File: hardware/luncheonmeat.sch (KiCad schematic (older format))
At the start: 55 parts, among them J1 USB_B_Micro, J2 Conn_02x03_Odd_Even, Q1 Q_PMOS_DGS, Q2 Q_PMOS_DGS, Q3 Q_PMOS_DGS, SW1 SW_Push, SW10 7, SW11 4, SW12 1, SW13 *, SW2 9, SW3 6, SW4 3, SW5 #, SW6 8, SW7 5, SW8 2, SW9 0, U1 ATmega328PB-AU, U2 lsd100bag-101-20, U3 lsd100bag-101-20, U4 lsd100bag-101-20, U5 FT230XS, Y1 16MHz

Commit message: Fix schematic, new board layout
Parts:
- removed C1, C10, C8, C9: 100n, Capacitor_SMD:C_0603_1608Metric_Pad1.05x0.95mm_HandSolder, symbol Device:C
- removed C2, C3: 22p, Capacitor_SMD:C_0603_1608Metric_Pad1.05x0.95mm_HandSolder, symbol Device:C
- removed D1: LED, Diode_SMD:D_0603_1608Metric_Pad1.05x0.95mm_HandSolder, symbol Device:LED
- removed J2: Conn_02x03_Odd_Even, Connector_PinHeader_2.54mm:PinHeader_2x03_P2.54mm_Vertical, symbol Connector_Generic:Conn_02x03_Odd_Even
- removed JP? (x2): Jumper_2_Open, symbol Jumper:Jumper_2_Open
- removed R1: 100k, Resistor_SMD:R_0603_1608Metric_Pad1.05x0.95mm_HandSolder, symbol Device:R
- removed R10, R11, R12, R13, R14, R15, R16, R7, R8, R9: 300R, Resistor_SMD:R_0603_1608Metric_Pad1.05x0.95mm_HandSolder, symbol Device:R
- removed R2, R3, R4: 1k, Resistor_SMD:R_0603_1608Metric_Pad1.05x0.95mm_HandSolder, symbol Device:R
- removed Y1: 16MHz, Crystal:Crystal_HC49-4H_Vertical, symbol Device:Crystal_Small
- added C1: 10nF, Capacitor_SMD:C_0805_2012Metric_Pad1.18x1.45mm_HandSolder, symbol Device:C_Small
- added C10, C6, C7, C8, C9: 100nF, Capacitor_SMD:C_0805_2012Metric_Pad1.18x1.45mm_HandSolder, symbol Device:C_Small
- added C12, C13: 22pF, Capacitor_SMD:C_0603_1608Metric_Pad1.08x0.95mm_HandSolder, symbol Device:C_Small
- added D1: G, LED_SMD:LED_0805_2012Metric_Castellated, symbol Device:LED_Small
- added D2: R, LED_SMD:LED_0805_2012Metric_Castellated, symbol Device:LED_Small
- added D3: Y, LED_SMD:LED_0805_2012Metric_Castellated, symbol Device:LED_Small
- added D4: D_Small, Diode_SMD:D_0805_2012Metric, symbol Device:D_Small
- added H1, H2, H3, H4, H5, H6: MH, MountingHole:MountingHole_3.2mm_M3_DIN965, symbol Mechanical:MountingHole
- added J2: AVR-ISP-6, Connector_IDC:IDC-Header_2x03_P2.54mm_Vertical, symbol Connector:AVR-ISP-6
- added R1: 1M, Resistor_SMD:R_0805_2012Metric_Pad1.20x1.40mm_HandSolder, symbol Device:R_Small
- added R10, R11, R12, R13, R14, R15, R16, R2, R7, R9: 300R, Resistor_SMD:R_0805_2012Metric_Pad1.20x1.40mm_HandSolder, symbol Device:R_Small
- added R17, R18: 0R, Resistor_SMD:R_0805_2012Metric_Pad1.20x1.40mm_HandSolder, symbol Device:R_Small
- added R19, R20, R21: 1k, Resistor_SMD:R_0805_2012Metric_Pad1.20x1.40mm_HandSolder, symbol Device:R_Small
- added R3, R4: 1.5k, Resistor_SMD:R_0805_2012Metric_Pad1.20x1.40mm_HandSolder, symbol Device:R_Small
- added R8: 10k, Resistor_SMD:R_0805_2012Metric_Pad1.20x1.40mm_HandSolder, symbol Device:R_Small
- added Y1: 8MHz, Crystal:Crystal_SMD_0603-4Pin_6.0x3.5mm_HandSoldering, symbol Device:Crystal_GND2_Small
- C2: renamed from C4; value 10n -> 10nF; footprint Capacitor_SMD:C_0603_1608Metric_Pad1.05x0.95mm_HandSolder -> Capacitor_SMD:C_0805_2012Metric_Pad1.18x1.45mm_HandSolder
- C3: renamed from C5; footprint Capacitor_SMD:C_0603_1608Metric_Pad1.05x0.95mm_HandSolder -> Capacitor_SMD:C_0805_2012Metric_Pad1.18x1.45mm_HandSolder
- C4: renamed from C6; footprint Capacitor_SMD:C_0603_1608Metric_Pad1.05x0.95mm_HandSolder -> Capacitor_SMD:C_0805_2012Metric_Pad1.18x1.45mm_HandSolder
- C5: renamed from C7; value 100n -> 100nF; footprint Capacitor_SMD:C_0603_1608Metric_Pad1.05x0.95mm_HandSolder -> Capacitor_SMD:C_0805_2012Metric_Pad1.18x1.45mm_HandSolder
- R5, R6: footprint Resistor_SMD:R_0603_1608Metric_Pad1.05x0.95mm_HandSolder -> Resistor_SMD:R_0805_2012Metric_Pad1.20x1.40mm_HandSolder
- SW13: renamed from SW1; footprint Connector_PinHeader_2.54mm:PinHeader_1x02_P2.54mm_Vertical -> Button_Switch_SMD:SW_Push_1P1T_NO_CK_KSC7xxJ
- renumbered SW10 to SW1, SW3 to SW10, SW4 to SW11, SW5 to SW12, SW11 to SW2, SW12 to SW3, SW13 to SW4, SW6 to SW5, SW7 to SW6, SW8 to SW7, SW9 to SW8, SW2 to SW9, U5 to U2, U2 to U3, U3 to U4, U4 to U5
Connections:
- net +5V: now also C10.1, C6.2, C8.2, C9.1, D4.1 (K), J2.2 (VCC), R8.2
- net MISO: now also J2.1 (MISO)
- net MOSI: now also J2.4 (MOSI)
- net RESET: now also J2.5 (~RST), R7.2
- net SCK: now also J2.3 (SCK)
- net SEG_A: now also R16.1
- net SEG_B: now also R15.1
- net SEG_C: now also R11.1
- net SEG_D: now also R10.1
- net SEG_E: now also R9.1
- net SEG_F: now also R13.1
- net SEG_G: now also R14.1
- net SEG_RDP: now also R12.1
- net SEG_SEL_0: now also R19.2
- net SEG_SEL_1: now also R20.2
- net SEG_SEL_2: now also R21.2
- net at U1.1 (PD3): now also R16.2
- net P_LED: now reaches U1.11 (PD7)
- net P_LED: now also R2.2
- net at U1.23 (PC0): now also R9.2
- net at U1.24 (PC1): now also R10.2
- net at U1.25 (PC2): now also R11.2
- net at U1.26 (PC3): now also R12.2
- net at U1.27 (PC4): now also R13.2
- net at U1.28 (PC5): now also R14.2
- net at U1.32 (PD2): now also R15.2
- net at U1.7 (XTAL1/PB6): now also C13.1, Y1.3
- net at U1.8 (XTAL2/PB7): now also C12.2, Y1.1
- net at Q1.1 (G): now also R19.1
- net at SW13.1: now also C7.2, D4.2 (A), R7.1, R8.1
- net at Q2.1 (G): now also R20.1
- net at Q3.1 (G): now also R21.1
- net +5VD: now reaches C5.2, U2.10 (3V3OUT), U2.11 (~RESET), U2.3 (VCCIO)
- net +5VD: now also R3.2, R4.2
- net at J1.6 (Shield): now also C1.2, R1.1
- net Earth renamed GND
- net GND: now also C1.1, C10.2, C12.1, C13.2, C6.1, C7.1, C8.1, C9.2, D1.1 (K), J2.6 (GND), R1.2, Y1.2
- net RX renamed RXD
- net RXD: now also R18.1; no longer U2.4 (RXD)
- net TX renamed TXD
- net TXD: now also R17.1; no longer U2.1 (TXD)
- new net: D1.2 (A), R2.1
- new net: D2.2 (A), R3.1
- new net: D3.2 (A), R4.1
- new net RX_F: D3.1 (K), R17.2, U2.4 (RXD)
- new net TX_F: D2.1 (K), R18.2, U2.1 (TXD)
- no-connect marks 0 -> 7
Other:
- moved on the sheet: C11, SW13

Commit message: v0.2.0, PCB board finished
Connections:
- net DR+: now also R5.2; no longer R6.2
- net DR-: now also R6.2; no longer R5.2
- net MISO: now also SW10.2, SW11.2, SW12.2, SW9.2
- net MOSI: now also SW5.2, SW6.2, SW7.2, SW8.2
- net P_LED: now also U1.23 (PC0); no longer U1.11 (PD7)
- net ROW_0: now also U1.13 (PB1); no longer U1.3 (PE0)
- net ROW_1: now also U1.12 (PB0); no longer U1.6 (PE1)
- net ROW_2: now also U1.11 (PD7); no longer U1.19 (PE2)
- net ROW_3: now also U1.10 (PD6); no longer U1.22 (PE3)
- net SEG_SEL_0: now also U1.28 (PC5); no longer U1.2 (PD4)
- net SEG_SEL_1: now also U1.32 (PD2); no longer U1.9 (PD5)
- net SEG_SEL_2: now also U1.9 (PD5); no longer U1.10 (PD6)
- net at U1.1 (PD3): now also R13.2; no longer R16.2
- net at R9.2: now also U1.24 (PC1); no longer U1.23 (PC0)
- net at R10.2: now also U1.25 (PC2); no longer U1.24 (PC1)
- net at R11.2: now also U1.26 (PC3); no longer U1.25 (PC2)
- net at R12.2: now also U1.27 (PC4); no longer U1.26 (PC3)
- net at R14.2: now also U1.2 (PD4); no longer U1.28 (PC5)
- net SEG_B_: now reaches R15.2
- net SEG_B_: now also U1.3 (PE0); no longer U1.32 (PD2)
- net USB+5V: now reaches C2.2, J1.1 (VBUS), L1.1
- removed net COL_0: SW10.2, SW11.2, SW12.2, SW9.2, U1.12 (PB0)
- removed net COL_1: SW5.2, SW6.2, SW7.2, SW8.2, U1.13 (PB1)
- new net SEG_A_: R16.2, U1.6 (PE1)
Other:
- moved on the sheet: C12, C13, R10, R11, R12, R13, R14, R15, R16, R9, Y1

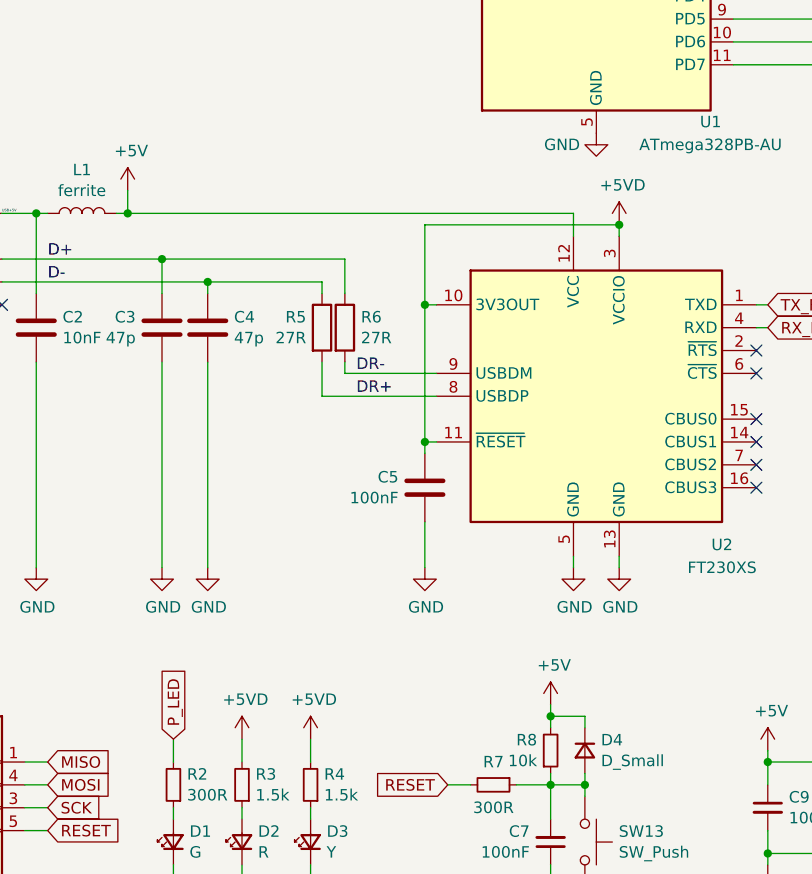
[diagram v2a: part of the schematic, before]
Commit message: v0.2.1 PCB Updated
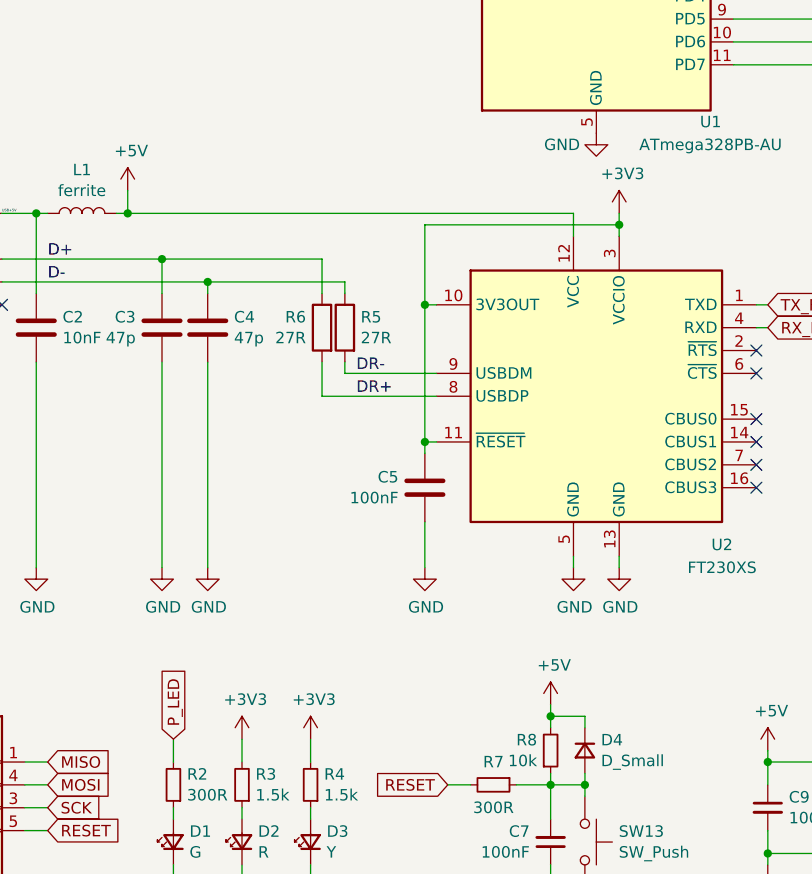
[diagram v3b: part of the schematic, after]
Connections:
- net DR+: now also R6.2; no longer R5.2
- net DR-: now also R5.2; no longer R6.2
- net +5VD renamed +3V3
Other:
- moved on the sheet: R5, R6
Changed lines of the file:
@@
 L Device:R R6
 U 1 1 5FC8EC48
+P 3350 5050
+F 0 "R6" H 3420 5096 50  0000 L CNN
+F 1 "27R" H 3420 5005 50  0000 L CNN
+F 2 "Resistor_SMD:R_0805_2012Metric_Pad1.20x1.40mm_HandSolder" V 3280 5050 50  0001 C CNN
+F 3 "~" H 3350 5050 50  0001 C CNN
+	1    3350 5050
+	-1   0    0    -1
+$EndComp
+$Comp
+L Device:R R5
+U 1 1 5FC8F2A2
 P 3450 5050
-F 0 "R6" H 3520 5096 50  0000 L CNN
-F 1 "27R" H 3520 5005 50  0000 L CNN
+F 0 "R5" H 3381 5096 50  0000 R CNN
+F 1 "27R" H 3381 5005 50  0000 R CNN
 F 2 "Resistor_SMD:R_0805_2012Metric_Pad1.20x1.40mm_HandSolder" V 3380 5050 50  0001 C CNN
 F 3 "~" H 3450 5050 50  0001 C CNN
 	1    3450 5050
-	1    0    0    -1
-$EndComp
-$Comp
-L Device:R R5
-U 1 1 5FC8F2A2
-P 3350 5050
-F 0 "R5" H 3281 5096 50  0000 R CNN
-F 1 "27R" H 3281 5005 50  0000 R CNN
-F 2 "Resistor_SMD:R_0805_2012Metric_Pad1.20x1.40mm_HandSolder" V 3280 5050 50  0001 C CNN
-F 3 "~" H 3350 5050 50  0001 C CNN
-	1    3350 5050
-	1    0    0    -1
-$EndComp
-Wire Wire Line
-	3350 4850 3350 4900
-Wire Wire Line
-	3450 4900 3450 4750
-Wire Wire Line
-	3450 4750 2650 4750
+	-1   0    0    -1
+$EndComp
+Wire Wire Line
+	3450 4850 3450 4900
+Wire Wire Line
+	3350 4900 3350 4750
+Wire Wire Line
+	3350 4750 2650 4750
 $Comp
 L Device:C C4
@@
 Connection ~ 2850 4850
 Wire Wire Line
-	2850 4850 3350 4850
+	2850 4850 3450 4850
 Wire Wire Line
 	2100 6100 2100 5200
@@
 Wire Wire Line
 	3300 6850 3300 6950
-$Comp
-L power:+5VD #PWR020
-U 1 1 6043532E
-P 4650 4600
-F 0 "#PWR020" H 4650 4450 50  0001 C CNN
-F 1 "+5VD" H 4665 4773 50  0000 C CNN
-F 2 "" H 4650 4600 50  0001 C CNN
-F 3 "" H 4650 4600 50  0001 C CNN
-	1    4650 4600
-	1    0    0    -1
-$EndComp
-Connection ~ 4650 4600
-$Comp
-L power:+5VD #PWR010
-U 1 1 604361C0
-P 3000 6850
-F 0 "#PWR010" H 3000 6700 50  0001 C CNN
-F 1 "+5VD" H 3015 7023 50  0000 C CNN
-F 2 "" H 3000 6850 50  0001 C CNN
-F 3 "" H 3000 6850 50  0001 C CNN
-	1    3000 6850
-	1    0    0    -1
-$EndComp
-$Comp
-L power:+5VD #PWR011
-U 1 1 60438C92
-P 3300 6850
-F 0 "#PWR011" H 3300 6700 50  0001 C CNN
-F 1 "+5VD" H 3315 7023 50  0000 C CNN
-F 2 "" H 3300 6850 50  0001 C CNN
-F 3 "" H 3300 6850 50  0001 C CNN
-	1    3300 6850
-	1    0    0    -1
-$EndComp
 Text GLabel 3000 7450 3    50   Input ~ 0
 TX_F
@@
 Entry Wire Line
 	3500 2950 3400 2850
+$Comp
+L power:+3V3 #PWR?
+U 1 1 60015479
+P 4650 4550
+F 0 "#PWR?" H 4650 4400 50  0001 C CNN
+F 1 "+3V3" H 4665 4723 50  0000 C CNN
+F 2 "" H 4650 4550 50  0001 C CNN
+F 3 "" H 4650 4550 50  0001 C CNN
+	1    4650 4550
+	1    0    0    -1
+$EndComp
+Wire Wire Line
+	4650 4550 4650 4600
 Wire Bus Line
 	6200 900  6200 1600
@@
 Wire Bus Line
 	8200 1600 8200 6000
+Connection ~ 4650 4600
+$Comp
+L power:+3V3 #PWR?
+U 1 1 6002C8D2
+P 3000 6850
+F 0 "#PWR?" H 3000 6700 50  0001 C CNN
+F 1 "+3V3" H 3015 7023 50  0000 C CNN
+F 2 "" H 3000 6850 50  0001 C CNN
+F 3 "" H 3000 6850 50  0001 C CNN
+	1    3000 6850
+	1    0    0    -1
+$EndComp
+$Comp
+L power:+3V3 #PWR?
+U 1 1 6003335C
+P 3300 6850
+F 0 "#PWR?" H 3300 6700 50  0001 C CNN
+F 1 "+3V3" H 3315 7023 50  0000 C CNN
+F 2 "" H 3300 6850 50  0001 C CNN
+F 3 "" H 3300 6850 50  0001 C CNN
+	1    3300 6850
+	1    0    0    -1
+$EndComp
 $EndSCHEMATC

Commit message: v0.2.2 PCB Updated
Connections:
- net +5V: now also Q1.2 (S), Q2.2 (S), Q3.2 (S); no longer Q1.3 (D), Q2.3 (D), Q3.3 (D)
- net at U3.3 (VDD), U3.8 (VDD): now also Q1.3 (D); no longer Q1.2 (S)
- net at U4.3 (VDD), U4.8 (VDD): now also Q2.3 (D); no longer Q2.2 (S)
- net at U5.3 (VDD), U5.8 (VDD): now also Q3.3 (D); no longer Q3.2 (S)
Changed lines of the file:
@@
 Sheet 1 1
 Title "Luncheomat"
-Date "2020-12-22"
-Rev "v0.2.0"
+Date "2021-01-15"
+Rev "v0.2.2"
 Comp "AlpsAlpine"
 Comment1 ""
@@
 F 3 "~" H 9000 4850 50  0001 C CNN
 	1    9000 4850
-	1    0    0    -1
+	1    0    0    1
 $EndComp
 Wire Wire Line
@@
 F 3 "~" H 9000 3100 50  0001 C CNN
 	1    9000 3100
-	1    0    0    -1
+	1    0    0    1
 $EndComp
 Wire Wire Line
@@
 F 3 "~" H 9000 1350 50  0001 C CNN
 	1    9000 1350
-	1    0    0    -1
+	1    0    0    1
 $EndComp
 Wire Wire Line
@@
 Wire Wire Line
 	4650 4550 4650 4600
+Connection ~ 4650 4600
+$Comp
+L power:+3V3 #PWR?
+U 1 1 6002C8D2
+P 3000 6850
+F 0 "#PWR?" H 3000 6700 50  0001 C CNN
+F 1 "+3V3" H 3015 7023 50  0000 C CNN
+F 2 "" H 3000 6850 50  0001 C CNN
+F 3 "" H 3000 6850 50  0001 C CNN
+	1    3000 6850
+	1    0    0    -1
+$EndComp
+$Comp
+L power:+3V3 #PWR?
+U 1 1 6003335C
+P 3300 6850
+F 0 "#PWR?" H 3300 6700 50  0001 C CNN
+F 1 "+3V3" H 3315 7023 50  0000 C CNN
+F 2 "" H 3300 6850 50  0001 C CNN
+F 3 "" H 3300 6850 50  0001 C CNN
+	1    3300 6850
+	1    0    0    -1
+$EndComp
 Wire Bus Line
 	6200 900  6200 1600
@@
 Wire Bus Line
 	8200 1600 8200 6000
-Connection ~ 4650 4600
-$Comp
-L power:+3V3 #PWR?
-U 1 1 6002C8D2
-P 3000 6850
-F 0 "#PWR?" H 3000 6700 50  0001 C CNN
-F 1 "+3V3" H 3015 7023 50  0000 C CNN
-F 2 "" H 3000 6850 50  0001 C CNN
-F 3 "" H 3000 6850 50  0001 C CNN
-	1    3000 6850
-	1    0    0    -1
-$EndComp
-$Comp
-L power:+3V3 #PWR?
-U 1 1 6003335C
-P 3300 6850
-F 0 "#PWR?" H 3300 6700 50  0001 C CNN
-F 1 "+3V3" H 3315 7023 50  0000 C CNN
-F 2 "" H 3300 6850 50  0001 C CNN
-F 3 "" H 3300 6850 50  0001 C CNN
-	1    3300 6850
-	1    0    0    -1
-$EndComp
 $EndSCHEMATC

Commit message: v0.2.3 PCB Updated, board step file generated
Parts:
- U3, U4, U5: footprint lsd100bag-101-20:lsd100bag-101-20 -> lsd100bag-101-20:lsd100bag-101
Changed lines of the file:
@@
 Title "Luncheomat"
 Date "2021-01-15"
-Rev "v0.2.2"
+Rev "v0.2.3"
 Comp "AlpsAlpine"
 Comment1 ""
@@
 F 0 "U5" H 9550 5100 50  0000 L CNN
 F 1 "lsd100bag-101-20" H 9200 5000 50  0000 L CNN
-F 2 "lsd100bag-101-20:lsd100bag-101-20" H 8750 5000 50  0001 C CNN
+F 2 "lsd100bag-101-20:lsd100bag-101" H 8750 5000 50  0001 C CNN
 F 3 "" H 8750 5000 50  0001 C CNN
 	1    9600 5650
@@
 F 0 "U4" H 9550 3350 50  0000 L CNN
 F 1 "lsd100bag-101-20" H 9200 3250 50  0000 L CNN
-F 2 "lsd100bag-101-20:lsd100bag-101-20" H 8750 3250 50  0001 C CNN
+F 2 "lsd100bag-101-20:lsd100bag-101" H 8750 3250 50  0001 C CNN
 F 3 "" H 8750 3250 50  0001 C CNN
 	1    9600 3900
@@
 F 0 "U3" H 9550 1600 50  0000 L CNN
 F 1 "lsd100bag-101-20" H 9200 1500 50  0000 L CNN
-F 2 "lsd100bag-101-20:lsd100bag-101-20" H 8750 1500 50  0001 C CNN
+F 2 "lsd100bag-101-20:lsd100bag-101" H 8750 1500 50  0001 C CNN
 F 3 "" H 8750 1500 50  0001 C CNN
 	1    9600 2150
@@
 	3500 2950 3400 2850
 $Comp
-L power:+3V3 #PWR?
+L power:+3V3 #PWR0101
 U 1 1 60015479
 P 4650 4550
-F 0 "#PWR?" H 4650 4400 50  0001 C CNN
+F 0 "#PWR0101" H 4650 4400 50  0001 C CNN
 F 1 "+3V3" H 4665 4723 50  0000 C CNN
 F 2 "" H 4650 4550 50  0001 C CNN
@@
 Connection ~ 4650 4600
 $Comp
-L power:+3V3 #PWR?
+L power:+3V3 #PWR0102
 U 1 1 6002C8D2
 P 3000 6850
-F 0 "#PWR?" H 3000 6700 50  0001 C CNN
+F 0 "#PWR0102" H 3000 6700 50  0001 C CNN
 F 1 "+3V3" H 3015 7023 50  0000 C CNN
 F 2 "" H 3000 6850 50  0001 C CNN
@@
 $EndComp
 $Comp
-L power:+3V3 #PWR?
+L power:+3V3 #PWR0103
 U 1 1 6003335C
 P 3300 6850
-F 0 "#PWR?" H 3300 6700 50  0001 C CNN
+F 0 "#PWR0103" H 3300 6700 50  0001 C CNN
 F 1 "+3V3" H 3315 7023 50  0000 C CNN
 F 2 "" H 3300 6850 50  0001 C CNN
